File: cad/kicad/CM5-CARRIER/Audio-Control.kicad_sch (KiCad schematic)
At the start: 38 parts, among them J901 AUDIO_8X8_TDM_CONTROL, J910 PJ-327A_CTIA, U900 CM5_AUDIO_OFFSHEET_PORT, U901 SN65LVDS047PW, U902 SN65LVDT2D, U903 PCA9306D, U910 LP5907MFX-3.3, U911 LP5907MFX-1.8, U912 ES8316, U913 TPA6132A2RTE, U914 TPD4E05U06DQA

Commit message: Complete A1 detailed carrier and audio capture
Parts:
- removed J910: PJ-327A_CTIA, symbol CM5Carrier:PJ_327A_CTIA
- removed U903: PCA9306D, symbol Interface:PCA9306D
- removed U910: LP5907MFX-3.3, symbol Regulator_Linear:LP5907MFX-3.3
- removed U912: ES8316, Package_DFN_QFN:QFN-32-1EP_4x4mm_P0.4mm_EP2.9x2.9mm_ThermalVias, symbol CM5Carrier:ES8316
- added C903, C904, C905, C906, C907, C908, C926, C927, C928, C929: 100nF, Capacitor_SMD:C_0402_1005Metric, symbol Device:C
- added C919: 4.7uF, Capacitor_SMD:C_0805_2012Metric, symbol Device:C
- added C922: 1uF, Capacitor_SMD:C_0603_1608Metric, symbol Device:C
- added J910: STX-353K7A-6N-KTTR, CM5Carrier:Kycon_STX-353K7A-6N-KTTR_PRELIMINARY, symbol CM5Carrier:Kycon_STX_353K7A_6N
- added R900: 0R star bond, Resistor_SMD:R_0603_1608Metric, symbol Device:R
- added R905, R906, R907, R908: 2.2k, Resistor_SMD:R_0603_1608Metric, symbol Device:R
- added R914: 10k, Resistor_SMD:R_0603_1608Metric, symbol Device:R
- added U903: PCA9517ADP, Package_SO:TSSOP-8_3x3mm_P0.65mm, symbol CM5Carrier:PCA9517ADP_A1
- added U904: PCA9306DP, Package_SO:TSSOP-8_3x3mm_P0.65mm, symbol Interface:PCA9306DP
- added U905: SN74AVC4T245PW, Package_SO:TSSOP-16_4.4x5mm_P0.65mm, symbol Logic_LevelTranslator:SN74AVC4T245PW
- added U906: SN74LVC1T45DCK, Package_TO_SOT_SMD:SOT-363_SC-70-6, symbol Logic_LevelTranslator:SN74LVC1T45DCK
- C901, C930: footprint (none) -> Capacitor_SMD:C_0402_1005Metric; MPN (none) -> C1005X7R1H104K050BB; Manufacturer (none) -> TDK
- C902, C910, C911, C912, C913, C920, C921: footprint (none) -> Capacitor_SMD:C_0603_1608Metric; MPN (none) -> GRM188R71A105KA61D; Manufacturer (none) -> Murata
- C914, C915, C916, C917, C918: footprint (none) -> Capacitor_SMD:C_0603_1608Metric; MPN (none) -> GRM188R61E106MA73D; Manufacturer (none) -> Murata
- C923, C924, C925: footprint (none) -> Capacitor_SMD:C_0603_1608Metric; MPN (none) -> GRM188R71A225KE15; Manufacturer (none) -> Murata
- J901: footprint (none) -> Connector_Molex_Milligrid:Molex_8783230xx_2x15_P2.0mm_Header_Vertical_Polarized_MountingPegs; MPN (none) -> 87832-6423; Manufacturer (none) -> Molex
- R901, R902, R903, R904, R910: footprint (none) -> Resistor_SMD:R_0603_1608Metric; MPN (none) -> RC0603FR-072K2L; Manufacturer (none) -> Yageo
- R911: footprint (none) -> Resistor_SMD:R_0603_1608Metric; MPN (none) -> RC0603FR-07330KL; Manufacturer (none) -> Yageo
- R912, R913: footprint (none) -> Resistor_SMD:R_0603_1608Metric; MPN (none) -> RC0603FR-07100KL; Manufacturer (none) -> Yageo
- U901: footprint (none) -> Package_SO:TSSOP-16_4.4x5mm_P0.65mm
- U902: footprint (none) -> Package_SO:SOIC-8_3.9x4.9mm_P1.27mm
- U910: renamed from C919; value 4.7uF -> LP5907MFX-3.3; footprint (none) -> Package_TO_SOT_SMD:SOT-23-5; symbol Device:C -> Regulator_Linear:LP5907MFX-3.3; MPN (none) -> LP5907MFX-3.3/NOPB; Manufacturer (none) -> Texas Instruments
- U911: footprint (none) -> Package_TO_SOT_SMD:SOT-23-5
- U912: renamed from C922; value 1uF -> ES8316; footprint (none) -> Package_DFN_QFN:QFN-32-1EP_4x4mm_P0.4mm_EP2.9x2.9mm_ThermalVias; symbol Device:C -> CM5Carrier:ES8316; MPN (none) -> ES8316; Manufacturer (none) -> Everest Semiconductor
- U913: footprint (none) -> Package_DFN_QFN:WQFN-16-1EP_3x3mm_P0.5mm_EP1.68x1.68mm_ThermalVias
- U914: footprint (none) -> Package_SON:USON-10_2.5x1.0mm_P0.5mm
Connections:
- net HPAMP_HPVDD is gone; now on net HEADSET_3V3: C923.1, U913.12 (HPVDD)
- net LOGIC_1V8 is gone; now on net LOGIC_3V3: R901.1, R902.1, R911.1
- net AUDIO_ENABLE: now also U903.5 (EN)
- net AUD_I2C_SCL: now also U903.7 (SCLB)
- net AUD_I2C_SDA: now also U903.6 (SDAB)
- net ES8316_ADCVREF: now also U912.24 (ADCVREF)
- net ES8316_CPBOT: now also U912.16 (CPBOT)
- net ES8316_CPTOP: now also U912.15 (CPTOP)
- net ES8316_CPVSS: now also U912.13 (CPVSSP)
- net ES8316_DACVREF: now also U912.21 (DACVREF)
- net ES8316_MICBIAS: now also U912.26 (MICBIAS)
- net ES8316_VMID: now also U912.25 (VMID), C919.1; no longer U910.1
- net GND: now also R900.1, U903.4 (GND); no longer C910.2, C911.2, C912.2, C913.2, R912.2, R913.2, U911.2 (GND), U913.6 (G0)
- net HEADSET_1V8: now also U912.14 (CPVDD), U912.3 (DVDD), U912.4 (PVDD), C904.1, C906.1, C908.1, C926.1, C927.1, C928.1, R905.1, R906.1, R914.1, U904.2 (VREF1), U905.16 (VCCB), U906.6 (VCCB)
- net HEADSET_3V3: now also U910.5 (OUT), U912.22 (AVDD), U913.6 (G0), C929.1; no longer U913.7 (G1)
- net HEADSET_AGND: now also C910.2, C911.2, C912.2, C913.2, R912.2, R913.2, U911.2 (GND), U912.17 (CPGND), U912.18 (CPGNDREF), U912.23 (AGND), U912.33 (E-PAD), U912.5 (DGND), U913.7 (G1), C903.2, C904.2, C905.2, C906.2, C907.2, C908.2, C919.2, C926.2, C927.2, C928.2, C929.2, J910.2 (R2_GND), J910.5 (SWITCH_A), R900.2, U904.1 (GND), U905.14 (2~{OE}), U905.15 (1~{OE}), U905.8 (GND), U905.9 (GND), U906.2 (GND), U906.5 (DIR)
- net HEADSET_HP_L: now also J910.4 (TIP_HP_L)
- net HEADSET_HP_R: now also J910.3 (R1_HP_R)
- net HEADSET_POWER_EN: now also U910.3 (EN)
- net HPAMP_CPN: now also C922.2; no longer U912.2
- net HPAMP_CPP: now also C922.1; no longer U912.1
- net HS_BCLK: now also U905.5 (1A2)
- net HS_CODEC_HP_L: now also U912.20 (LOUT)
- net HS_CODEC_HP_R: now also U912.19 (ROUT)
- net HS_I2C_SCL: now also R907.2, U904.6 (SCL2)
- net HS_I2C_SDA: now also R908.2, U904.5 (SDA2)
- net HS_JACK_DET_N: now also J910.6 (SWITCH_B)
- net HS_LRCK: now also U905.6 (2A1)
- net HS_MCLK: now also U905.4 (1A1)
- net HS_MIC_INPUT: now also U912.27 (RIN2)
- net HS_MIC_JACK: now also J910.1 (SLEEVE_MIC)
- net HS_SDIN_FROM_CODEC: now also U906.3 (A)
- net HS_SDOUT_TO_CODEC: now also U905.7 (2A2)
- net LOGIC_3V3: now also C903.1, C905.1, C907.1, R907.1, R908.1, U903.1 (VCCA), U903.8 (VCCB), U904.7 (VREF2), U904.8 (EN), U905.1 (VCCA), U905.2 (1DIR), U905.3 (2DIR), U906.1 (VCCA)
- net SYS_5V15: now also U910.1 (IN)
- net SYS_I2C7_SCL: now also U903.2 (SCLA)
- net SYS_I2C7_SDA: now also U903.3 (SDAA)
- new net ES8316_CE: R914.2, U912.31 (CE)
- new net HS_CODEC_BCLK: U905.12 (1B2), U912.6 (SCLK)
- new net HS_CODEC_I2C_SCL: R905.2, U904.3 (SCL1), U912.1 (CCLK)
- new net HS_CODEC_I2C_SDA: R906.2, U904.4 (SDA1), U912.32 (CDATA)
- new net HS_CODEC_LRCK: U905.11 (2B1), U912.8 (DLRCK)
- new net HS_CODEC_MCLK: U905.13 (1B1), U912.2 (MCLK)
- new net HS_CODEC_SDIN: U906.4 (B), U912.9 (ASDOUT)
- new net HS_CODEC_SDOUT: U905.10 (2B2), U912.7 (DSDIN)
- no-connect marks 13 -> 15
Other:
- note added: "2. I2S1 HEADSET LEVEL TRANSLATION"
- note added: "3. DEDICATED LOW-NOISE HEADSET RAILS"
- note added: "4. ES8316 I2S1 HEADSET CODEC"
- note added: "5. TPA6132A2 HEADPHONE AMPLIFIER"
- note added: "6. CTIA HEADSET JACK, MIC BIAS, DETECT, AND ESD"
- note added: "7. HEADSET CONTROL POLICY"
- note added: "CE is pulled to 1.8 V; all ES8316 digital pins are translated. Decoupling follows the Radxa reference topology."
- note added: "CM5 audio GPIO is 3.3 V. ES8316 digital pins remain entirely in the translated 1.8 V domain."
- note added: "CTIA contact map: tip=L, ring1=R, ring2=GND, sleeve=MIC. Verify isolated switch polarity on a Kycon sample."
- note added: "Firmware must debounce HS_JACK_DET_N and perform pop-free mute before any route change."
- note added: "G0=1 and G1=0 select 0 dB gain. EN remains software-controlled for pop-free mute."
- note added: "HEADSET_POWER_EN and HEADSET_AMP_EN default low so the codec and amplifier remain muted during boot."
- note added: "J910 is routable for prototype capture, but its drawing-derived footprint is blocked from production until sample/coupon sign-off."
- note added: "R900 is the only headset analog-ground bond. Do not create a second PCB or chassis bond."
- note added: "Sequence: enable rails, configure ES8316, enable TPA6132A2, then ramp software volume."
- note removed: "2. DEDICATED LOW-NOISE HEADSET RAILS"
- note removed: "3. ES8316 I2S1 HEADSET CODEC"
- note removed: "4. TPA6132A2 HEADPHONE AMPLIFIER"
- note removed: "5. CTIA HEADSET JACK, MIC BIAS, DETECT, AND ESD"
- note removed: "6. HEADSET I2C AND CONTROL POLICY"
- note removed: "CTIA mapping is locked. The PJ-327A supplier footprint still requires mechanical verification before PCB release."
- note removed: "Codec pinout and baseline decoupling follow Radxa CM5 IO V2.2; validate Everest production datasheet values before release."
- note removed: "ES8316 is controlled on HS_I2C_SCL/HS_I2C_SDA. No GPIO-expander interrupt is required; status is polled."
- note removed: "G0=0 and G1=1 strap the amplifier for 0 dB gain. EN remains software-controlled for pop-free mute."
- note removed: "HEADSET_POWER_EN and HEADSET_AMP_EN default low through 100k pulldowns so the jack remains muted during boot."
- note removed: "LP5907 rails are dedicated to the codec/headphone path. HEADSET_POWER_EN comes from the GPIO expander."
- note removed: "Sequence: enable codec rails, configure ES8316, enable TPA6132A2, then ramp software volume."

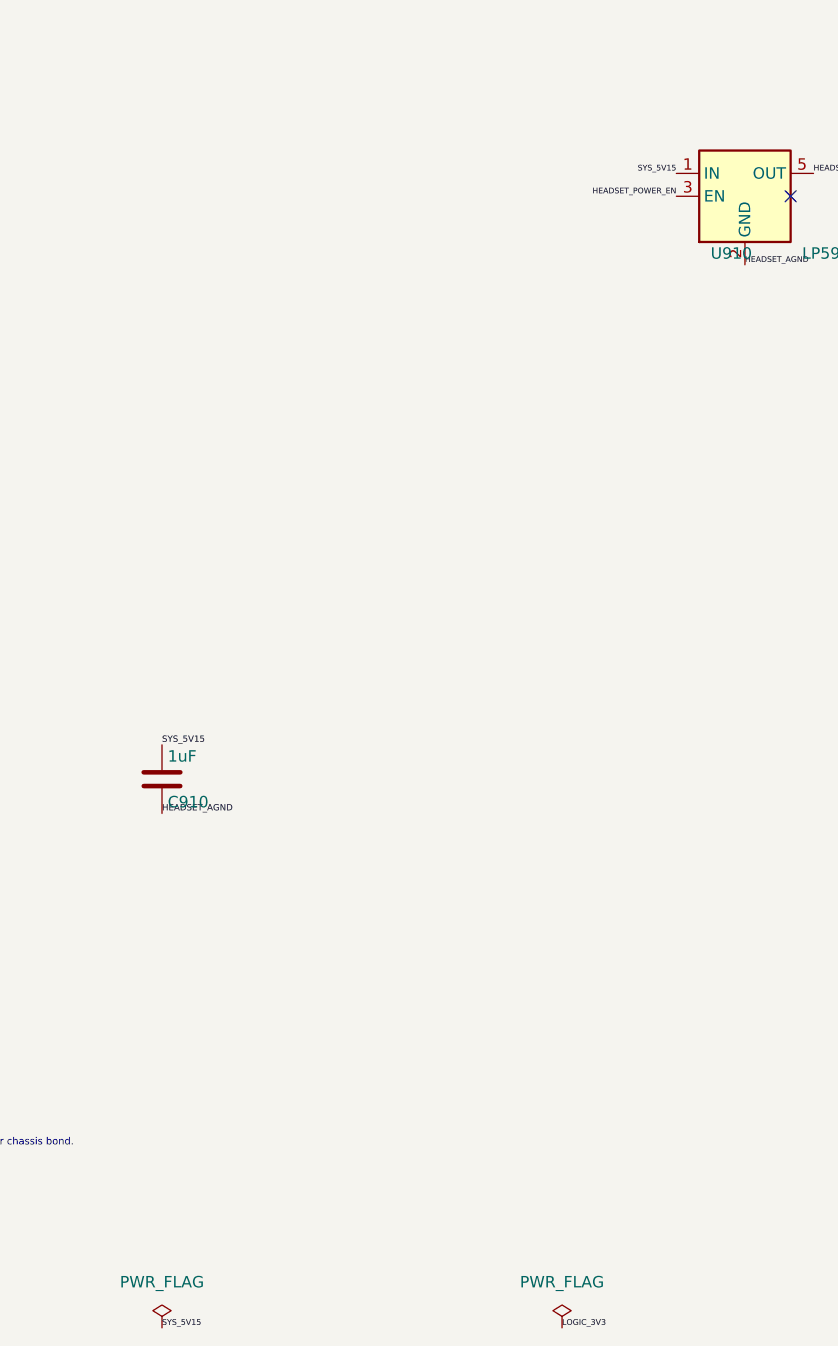
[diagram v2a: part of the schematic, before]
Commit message: Lock CM5 power and radio interfaces before routing
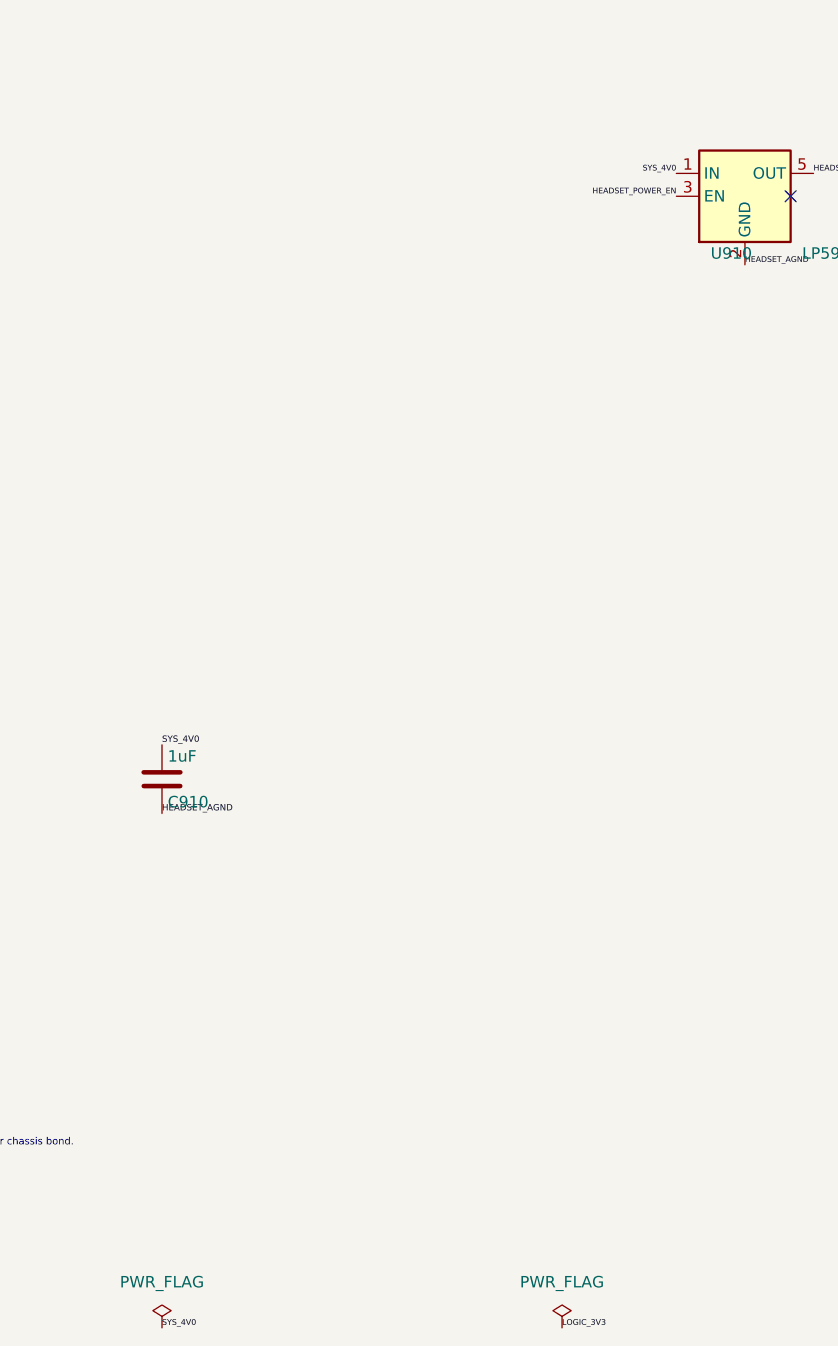
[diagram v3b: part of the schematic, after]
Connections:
- net SYS_5V15 renamed SYS_4V0
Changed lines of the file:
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@@
 		)
 	)
-	(label "SYS_5V15"
+	(label "SYS_4V0"
 		(at 137.16 697.23 0.0000)
 		(effects
@@
 		)
 	)
-	(label "SYS_5V15"
+	(label "SYS_4V0"
 		(at 80.01 760.73 0.0000)
 		(effects
@@
 		)
 	)
-	(label "SYS_5V15"
+	(label "SYS_4V0"
 		(at 80.01 825.5 0.0000)
 		(effects

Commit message: Audit schematic logic against controlled datasheets
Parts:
- added R909: 200k, Resistor_SMD:R_0603_1608Metric, symbol Device:R
- U900: now left out of the parts list
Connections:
- net LOGIC_3V3: now also R909.1; no longer U904.7 (VREF2), U904.8 (EN)
- net AUD_DAC_MUTE_N renamed AUD_DAC_MUTE_CMD_N
- new net HS_I2C_BIAS: R909.2, U904.7 (VREF2), U904.8 (EN)
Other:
- note added: "PCA9306 VREF2 and EN share HS_I2C_BIAS through the required 200 k pull-up to 3.3 V."

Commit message: Implement direct socketed dual-SIM daughterboard
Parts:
- removed C903, C904, C905: 100nF, Capacitor_SMD:C_0402_1005Metric, symbol Device:C
- removed C910, C920, C921, C922: 1uF, Capacitor_SMD:C_0603_1608Metric, symbol Device:C
- removed C914, C915, C916: 10uF, Capacitor_SMD:C_0603_1608Metric, symbol Device:C
- removed R902, R906, R910: 2.2k, Resistor_SMD:R_0603_1608Metric, symbol Device:R
- removed U902: SN65LVDT2D, Package_SO:SOIC-8_3.9x4.9mm_P1.27mm, symbol Interface:SN65LVDT2D
- removed U903: PCA9517ADP, Package_SO:TSSOP-8_3x3mm_P0.65mm, symbol CM5Carrier:PCA9517ADP_A1
- removed U904: PCA9306DP, Package_SO:TSSOP-8_3x3mm_P0.65mm, symbol Interface:PCA9306DP
- removed U911: LP5907MFX-1.8, Package_TO_SOT_SMD:SOT-23-5, symbol Regulator_Linear:LP5907MFX-1.8
- added C901, C906, C907, C908, C928, C929: 100nF, Capacitor_SMD:C_0402_1005Metric, symbol Device:C
- added C913: 1uF, Capacitor_SMD:C_0603_1608Metric, symbol Device:C
- added C923, C924, C925: 2.2uF, Capacitor_SMD:C_0603_1608Metric, symbol Device:C
- added J901: AUDIO_8X8_TDM_CONTROL, Connector_Molex_Milligrid:Molex_8783230xx_2x15_P2.0mm_Header_Vertical_Polarized_MountingPegs, symbol Connector_Generic:Conn_02x15_Odd_Even
- added R900: 0R star bond, Resistor_SMD:R_0603_1608Metric, symbol Device:R
- added R904, R908: 2.2k, Resistor_SMD:R_0603_1608Metric, symbol Device:R
- added R909: 200k, Resistor_SMD:R_0603_1608Metric, symbol Device:R
- added R914: 10k, Resistor_SMD:R_0603_1608Metric, symbol Device:R
- added U914: TPD4E05U06DQA, Package_SON:USON-10_2.5x1.0mm_P0.5mm, symbol Power_Protection:TPD4E05U06DQA
- C911: renamed from R900; value 0R star bond -> 1uF; footprint Resistor_SMD:R_0603_1608Metric -> Capacitor_SMD:C_0603_1608Metric; symbol Device:R -> Device:C; MPN RC0603JR-070RL -> GRM188R71A105KA61D; Manufacturer Yageo -> Murata
- C916: renamed from C919; value 4.7uF -> 10uF; footprint Capacitor_SMD:C_0805_2012Metric -> Capacitor_SMD:C_0603_1608Metric; MPN GRM21BR71A475KA73L -> GRM188R61E106MA73D
- C917: renamed from C926; value 100nF -> 10uF; footprint Capacitor_SMD:C_0402_1005Metric -> Capacitor_SMD:C_0603_1608Metric; MPN C1005X7R1H104K050BB -> GRM188R61E106MA73D; Manufacturer TDK -> Murata
- C918: renamed from C927; value 100nF -> 10uF; footprint Capacitor_SMD:C_0402_1005Metric -> Capacitor_SMD:C_0603_1608Metric; MPN C1005X7R1H104K050BB -> GRM188R61E106MA73D; Manufacturer TDK -> Murata
- C919: renamed from C928; value 100nF -> 4.7uF; footprint Capacitor_SMD:C_0402_1005Metric -> Capacitor_SMD:C_0805_2012Metric; MPN C1005X7R1H104K050BB -> GRM21BR71A475KA73L; Manufacturer TDK -> Murata
- C920: renamed from C923; value 2.2uF -> 1uF; MPN GRM188R71A225KE15 -> GRM188R71A105KA61D
- C921: renamed from C924; value 2.2uF -> 1uF; MPN GRM188R71A225KE15 -> GRM188R71A105KA61D
- C922: renamed from C925; value 2.2uF -> 1uF; MPN GRM188R71A225KE15 -> GRM188R71A105KA61D
- C927: renamed from R914; value 10k -> 100nF; footprint Resistor_SMD:R_0603_1608Metric -> Capacitor_SMD:C_0402_1005Metric; symbol Device:R -> Device:C; MPN RC0603FR-0710KL -> C1005X7R1H104K050BB; Manufacturer Yageo -> TDK
- R902: renamed from J901; value AUDIO_8X8_TDM_CONTROL -> 2.2k; footprint Connector_Molex_Milligrid:Molex_8783230xx_2x15_P2.0mm_Header_Vertical_Polarized_MountingPegs -> Resistor_SMD:R_0603_1608Metric; symbol Connector_Generic:Conn_02x15_Odd_Even -> Device:R; MPN 87832-6423 -> RC0603FR-072K2L; Manufacturer Molex -> Yageo
- R906: renamed from R909; value 200k -> 2.2k; MPN RC0603FR-07200KL -> RC0603FR-072K2L
- R910: renamed from U914; value TPD4E05U06DQA -> 2.2k; footprint Package_SON:USON-10_2.5x1.0mm_P0.5mm -> Resistor_SMD:R_0603_1608Metric; symbol Power_Protection:TPD4E05U06DQA -> Device:R; MPN TPD4E05U06DQAR -> RC0603FR-072K2L; Manufacturer Texas Instruments -> Yageo
- U902: renamed from C901; value 100nF -> SN65LVDT2D; footprint Capacitor_SMD:C_0402_1005Metric -> Package_SO:SOIC-8_3.9x4.9mm_P1.27mm; symbol Device:C -> Interface:SN65LVDT2D; MPN C1005X7R1H104K050BB -> SN65LVDT2DR; Manufacturer TDK -> Texas Instruments
- U903: renamed from R901; value 2.2k -> PCA9517ADP; footprint Resistor_SMD:R_0603_1608Metric -> Package_SO:TSSOP-8_3x3mm_P0.65mm; symbol Device:R -> CM5Carrier:PCA9517ADP_A1; MPN RC0603FR-072K2L -> PCA9517ADP,118; Manufacturer Yageo -> NXP
- U904: renamed from R905; value 2.2k -> PCA9306DP; footprint Resistor_SMD:R_0603_1608Metric -> Package_SO:TSSOP-8_3x3mm_P0.65mm; symbol Device:R -> Interface:PCA9306DP; MPN RC0603FR-072K2L -> PCA9306DP,118; Manufacturer Yageo -> NXP
- U911: renamed from C911; value 1uF -> LP5907MFX-1.8; footprint Capacitor_SMD:C_0603_1608Metric -> Package_TO_SOT_SMD:SOT-23-5; symbol Device:C -> Regulator_Linear:LP5907MFX-1.8; MPN GRM188R71A105KA61D -> LP5907MFX-1.8/NOPB; Manufacturer Murata -> Texas Instruments
- renumbered C906 to C903, C907 to C904, C908 to C905, C913 to C910, C917 to C914, C918 to C915, C929 to C926, R904 to R901, R908 to R905
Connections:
- net AUDIO_ENABLE: now also U903.5 (EN), J901.24 (Pin_24); no longer R902.24 (Pin_24)
- net AUDIO_PRESENT_N: now also J901.23 (Pin_23); no longer R902.23 (Pin_23)
- net AUD_ADC_RST_N: now also J901.19 (Pin_19); no longer R902.19 (Pin_19)
- net AUD_ADC_SDOUT: now also U902.7 (R)
- net AUD_ADC_SDOUT_N: now also U902.1 (B), J901.14 (Pin_14); no longer R902.14 (Pin_14)
- net AUD_ADC_SDOUT_P: now also U902.2 (A), J901.13 (Pin_13); no longer R902.13 (Pin_13)
- net AUD_BCLK_N: now also J901.6 (Pin_6); no longer R902.6 (Pin_6)
- net AUD_BCLK_P: now also J901.5 (Pin_5); no longer R902.5 (Pin_5)
- net AUD_DAC_MUTE_CMD_N: now also J901.21 (Pin_21); no longer R902.21 (Pin_21)
- net AUD_DAC_RST_N: now also J901.20 (Pin_20); no longer R902.20 (Pin_20)
- net AUD_DAC_SDIN_N: now also J901.12 (Pin_12); no longer R902.12 (Pin_12)
- net AUD_DAC_SDIN_P: now also J901.11 (Pin_11); no longer R902.11 (Pin_11)
- net AUD_FSYNC_N: now also J901.8 (Pin_8); no longer R902.8 (Pin_8)
- net AUD_FSYNC_P: now also J901.7 (Pin_7); no longer R902.7 (Pin_7)
- net AUD_I2C_SCL: now also U903.7 (SCLB), J901.17 (Pin_17); no longer R902.17 (Pin_17)
- net AUD_I2C_SDA: now also U903.6 (SDAB), J901.18 (Pin_18), R904.2; no longer R901.2, R902.18 (Pin_18)
- net AUD_IRQ_N: now also J901.22 (Pin_22); no longer R902.22 (Pin_22)
- net AUD_MCLK_N: now also J901.2 (Pin_2); no longer R902.2 (Pin_2)
- net AUD_MCLK_P: now also J901.1 (Pin_1); no longer R902.1 (Pin_1)
- net ES8316_ADCVREF: now also C918.1; no longer C915.1
- net ES8316_CE: now also R914.2; no longer C927.2
- net ES8316_CPBOT: now also C916.2
- net ES8316_CPTOP: now also C916.1
- net ES8316_CPVSS: now also C914.1
- net ES8316_DACVREF: now also C917.1; no longer C914.1
- net ES8316_MICBIAS: now also R910.1
- net ES8316_VMID: now also C919.1; no longer C916.1
- net GND: now also U902.5 (GND), U903.4 (GND), C901.2, J901.10 (Pin_10), J901.15 (Pin_15), J901.16 (Pin_16), J901.26 (Pin_26), J901.29 (Pin_29), J901.3 (Pin_3), J901.30 (Pin_30), J901.4 (Pin_4), J901.9 (Pin_9), R900.1; no longer C911.1, R902.10 (Pin_10), R902.15 (Pin_15), R902.16 (Pin_16), R902.26 (Pin_26), R902.29 (Pin_29), R902.3 (Pin_3), R902.30 (Pin_30), R902.4 (Pin_4), R902.9 (Pin_9), U902.2
- net HEADSET_1V8: now also C904.1, C915.1, C926.1, R905.1, R906.1, U904.2 (VREF1), U911.5 (OUT), C906.1, C908.1, C913.1, C928.1, R914.1; no longer C903.1, C905.1, C910.1, C917.1, C918.1, C919.1, U904.1
- net HEADSET_3V3: now also C911.1, C923.1, C925.1, C929.1; no longer C920.1, C922.1, C926.1
- net HEADSET_AGND: now also C927.2, U904.1 (GND), C906.2, C907.2, C908.2, C913.2, C923.2, C924.2, C925.2, C928.2, C929.2, R900.2, U914.3 (GND), U914.8 (GND); no longer C916.2, C920.2, C921.2, C922.2, R910.3 (GND), R910.8 (GND)
- net HEADSET_HP_L: now also U914.1 (D1+); no longer R910.1 (D1+)
- net HEADSET_HP_R: now also U914.2 (D1-); no longer R910.2 (D1-)
- net HEADSET_POWER_EN: now also U911.3 (EN)
- net HPAMP_CPN: now also C922.2
- net HPAMP_CPP: now also C922.1
- net HPAMP_HPVSS: now also C924.1; no longer C921.1
- net HPAMP_IN_L: now also C920.2
- net HPAMP_IN_R: now also C921.2
- net HS_CODEC_HP_L: now also C920.1
- net HS_CODEC_HP_R: now also C921.1
- net HS_CODEC_I2C_SCL: now also R905.2, U904.3 (SCL1); no longer U904.2
- net HS_CODEC_I2C_SDA: now also R906.2, U904.4 (SDA1)
- net HS_I2C_BIAS: now also U904.7 (VREF2), U904.8 (EN), R909.2; no longer R906.2
- net HS_I2C_SCL: now also U904.6 (SCL2)
- net HS_I2C_SDA: now also U904.5 (SDA2), R908.2; no longer R905.2
- net HS_JACK_DET_N: now also U914.5 (D2-); no longer R910.5 (D2-)
- net HS_MIC_JACK: now also R910.2, U914.4 (D2+); no longer R910.4 (D2+)
- net LOGIC_3V3: now also C903.1, C905.1, R902.1, U902.8 (V_{CC}), U903.8 (VCCB), C901.1, C907.1, J901.25 (Pin_25), R904.1, R908.1, R909.1; no longer C904.1, R902.25 (Pin_25), R905.1, R906.1, U902.1
- net SYS_4V0: now also C910.1
- net SYS_I2C7_SCL: now also R901.2
- net SYS_I2C7_SDA: now also R902.2, U903.3 (SDAA)
- net TDM_SPARE_1: now also J901.27 (Pin_27); no longer R902.27 (Pin_27)
- net TDM_SPARE_2: now also J901.28 (Pin_28); no longer R902.28 (Pin_28)
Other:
- moved on the sheet: C903, C904, C905, C910, C914, C915, C916, C917, C918, C919, C920, C921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
